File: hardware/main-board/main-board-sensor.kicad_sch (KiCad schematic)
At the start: 16 parts, among them J4 Conn_01x04, U1 TSL2585, U3 MIC4812, U7 MCP9808

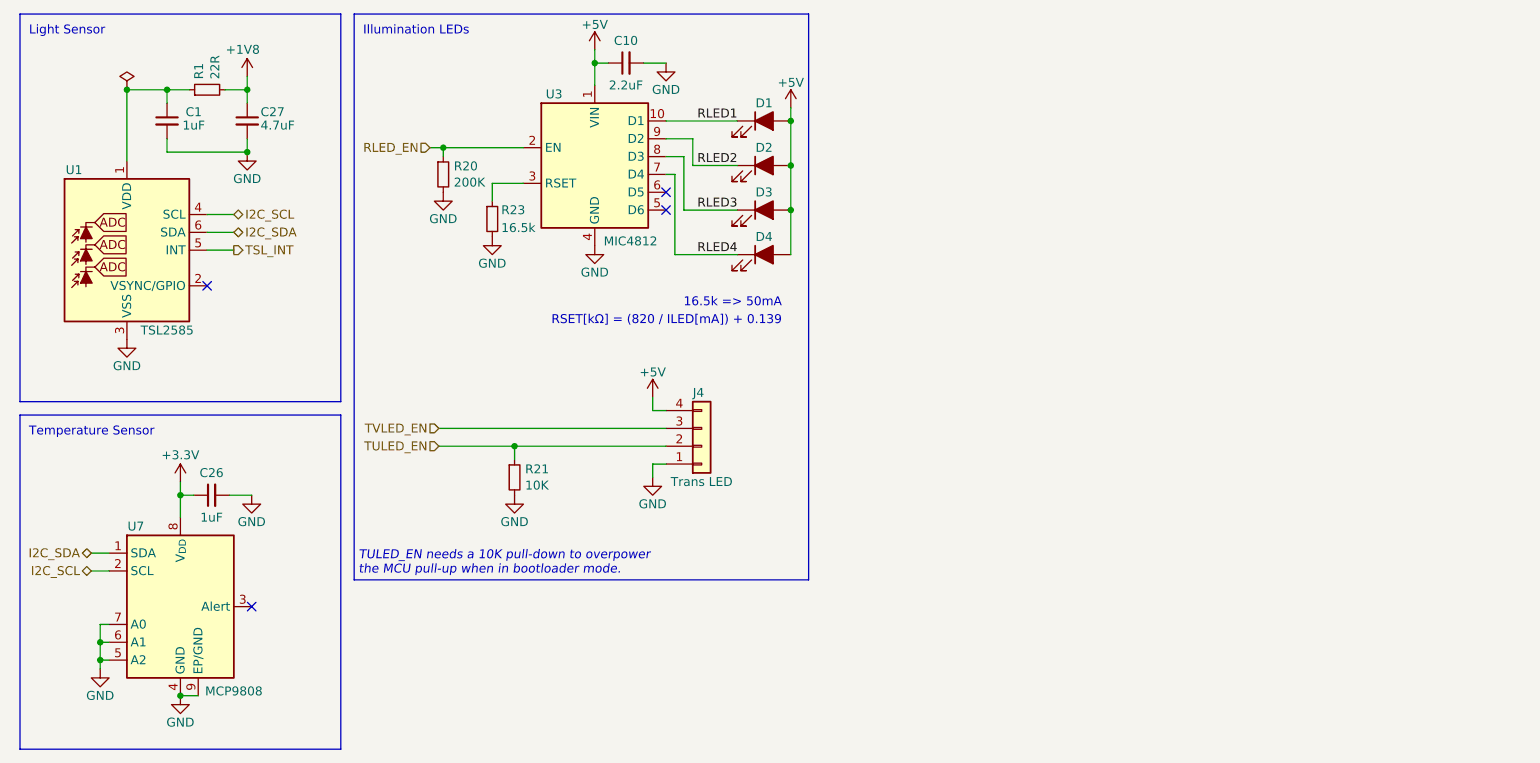
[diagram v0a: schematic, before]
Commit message: Implement VSYNC reference signal
Adds a 32.768kHz oscillator and a binary counter to divide it, providing
a stable 128Hz signal routed to the sensor's VSYNC pin.
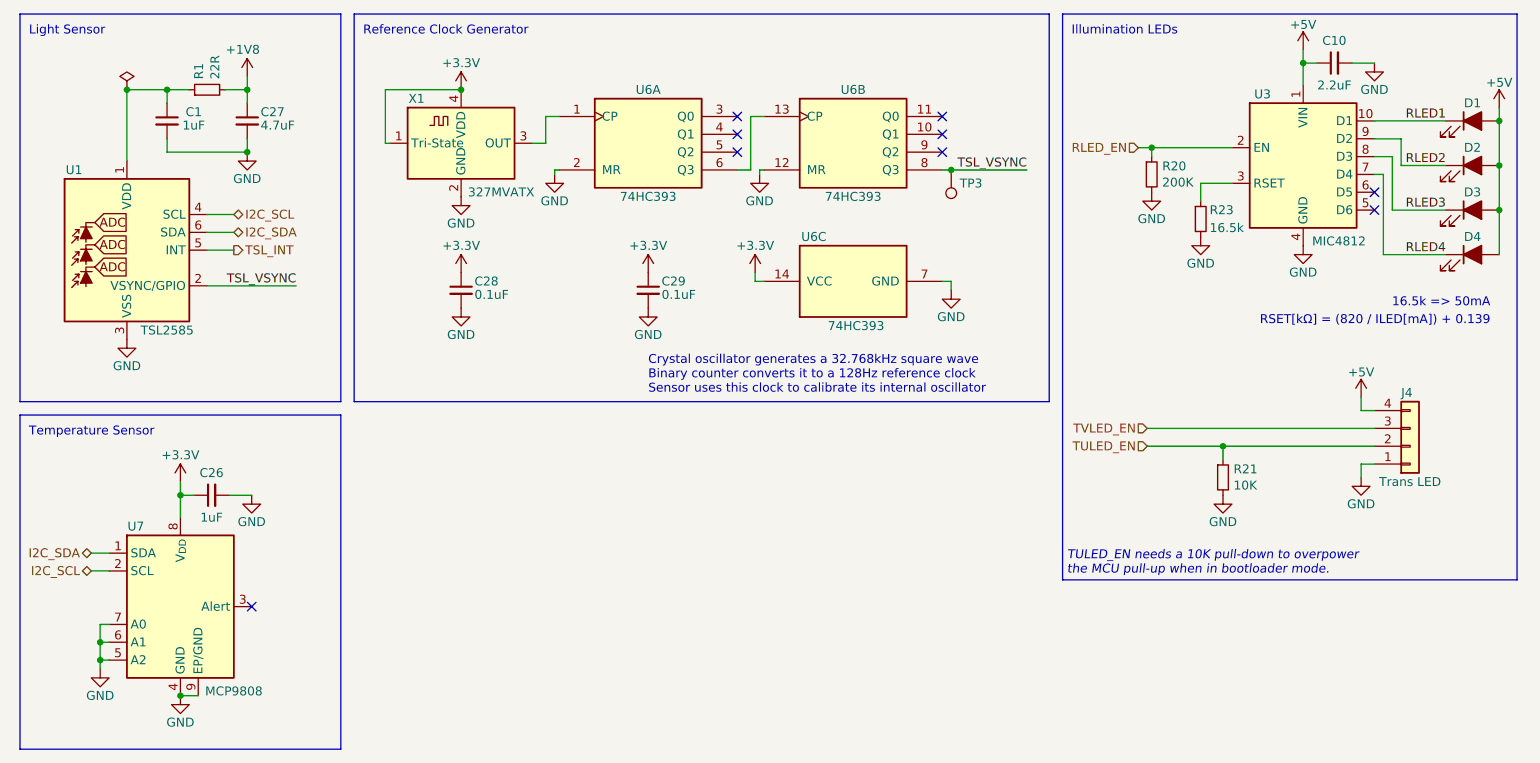
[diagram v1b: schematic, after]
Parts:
- added C28, C29: 0.1uF, Capacitor_SMD:C_0603_1608Metric, symbol Device:C_Small
- added TP3: 1.8V, TestPoint:TestPoint_Pad_D1.0mm, symbol Connector:TestPoint
- added U6: 74HC393, lib_fp:DHVQFN-14-1EP_2.5x3mm_P0.5mm_EP1x1.5mm, symbol 74xx:74LS393
- added X1: 327MVATX, lib_fp:Oscillator_SMD_ECS_327MVATX-2-4Pin_2.5x2.0mm, symbol Oscillator:ECS-2520MV-xxx-xx
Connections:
- net +3.3V: now also C28.1, C29.1, U6.14 (VCC), X1.1 (Tri-State), X1.4 (VDD)
- net GND: now also C28.2, C29.2, U6.12 (MR), U6.2 (MR), U6.7 (GND), X1.2 (GND)
- net TSL_VSYNC: now reaches U1.2 (VSYNC/GPIO)
- net TSL_VSYNC: now also TP3.1, U6.8 (Q3)
- new net: U6.13 (CP), U6.6 (Q3)
- new net: U6.1 (CP), X1.3 (OUT)
- no-connect marks 4 -> 9
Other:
- note added: "Crystal oscillator generates a 32.768kHz square wave Binary counter converts it to a 128Hz reference clock Sensor uses this clock to calibrate its internal oscillator"
- note added: "Reference Clock Generator"
- moved on the sheet: C10, D1, D2, D3, D4, J4, R20, R21, R23, U3

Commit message: Final tweaks for Rev C manufacture
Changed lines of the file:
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@@
 	(title_block
 		(title "Printalyzer UV/VIS Densitometer - Main Board")
-		(date "2024-09-04")
+		(date "2024-09-24")
 		(rev "C")
 		(company "Dektronics, Inc.")
@@
 	(rectangle
 		(start 163.195 14.605)
-		(end 227.965 95.25)
-		(stroke
-			(width 0)
+		(end 229.235 95.25)
+		(stroke
+			(width 0)

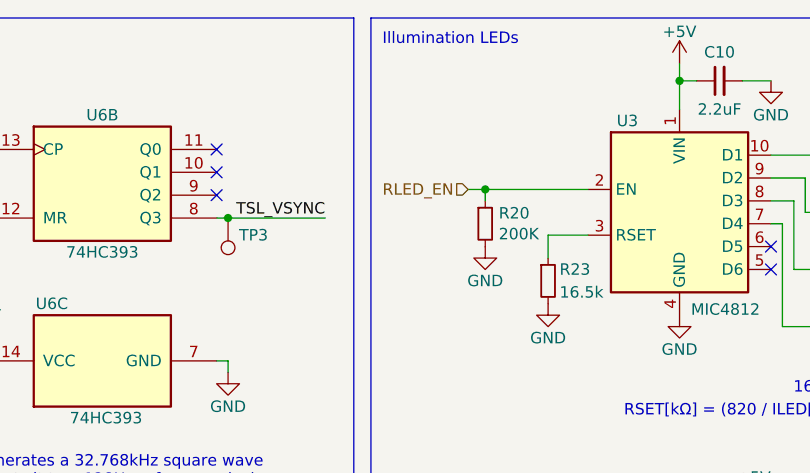
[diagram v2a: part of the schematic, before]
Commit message: Fix net name for reflection LEDs
This should match the identifer used in the firmware, for consistency
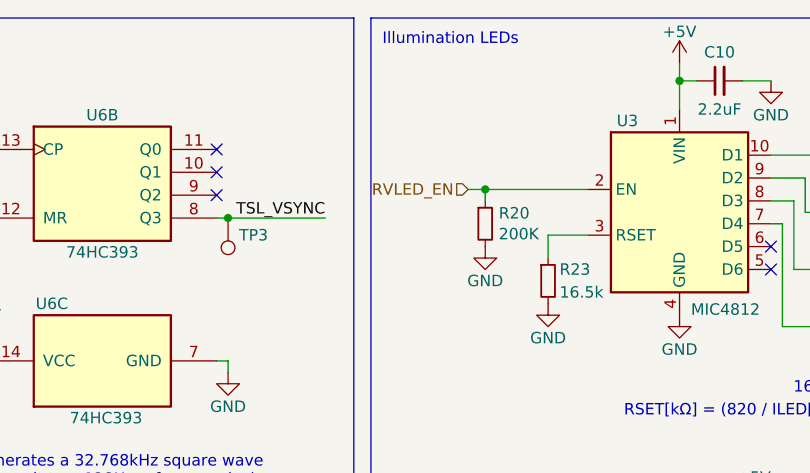
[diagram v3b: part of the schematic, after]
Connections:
- net RLED_EN renamed RVLED_EN
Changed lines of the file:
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@@
 		)
 	)
-	(hierarchical_label "RLED_EN"
+	(hierarchical_label "RVLED_EN"
 		(shape input)
 		(at 173.99 33.655 180)

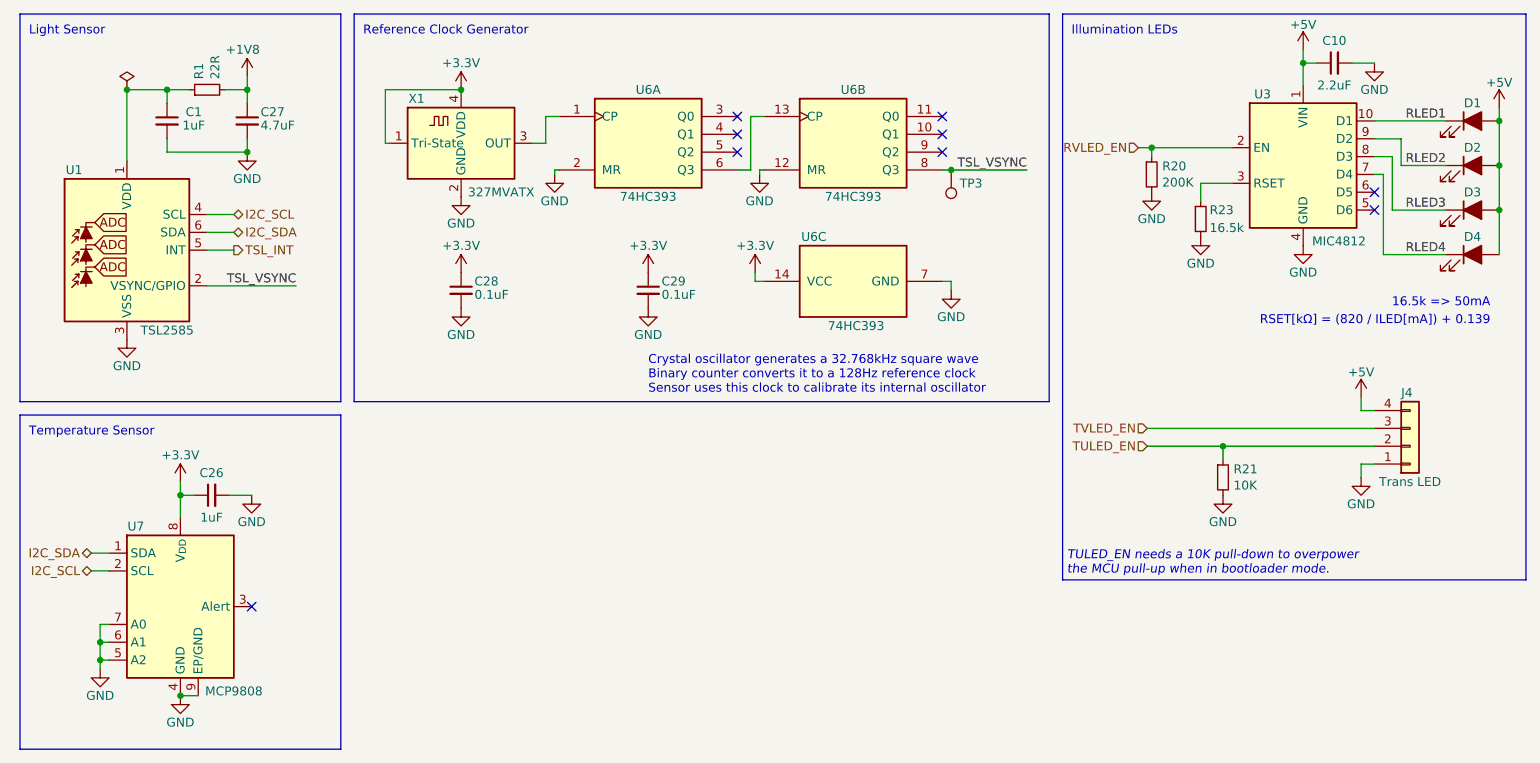
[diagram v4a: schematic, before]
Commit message: Remove crystal reference and reroute VSYNC pin
In testing with Rev C hardware, it was determined that using the VSYNC
pin to calibrate the TSL2585's internal oscillator can actually
introduce more instability in sensor timing than would otherwise exist.
Furthermore, the most likely factor affecting oscillator stability is
temperature, which we're already planning to correct for.

Thus these extra components should be removed from the design.

For the sake of future-proofing, the VSYNC pin is now rounded directly
to the MCU (though a pull-up resistor), in case someday it is decided to
use this as a measurement trigger. It is also likely this pin will never
be used, but it doesn't really hurt to do this.

Fix #2
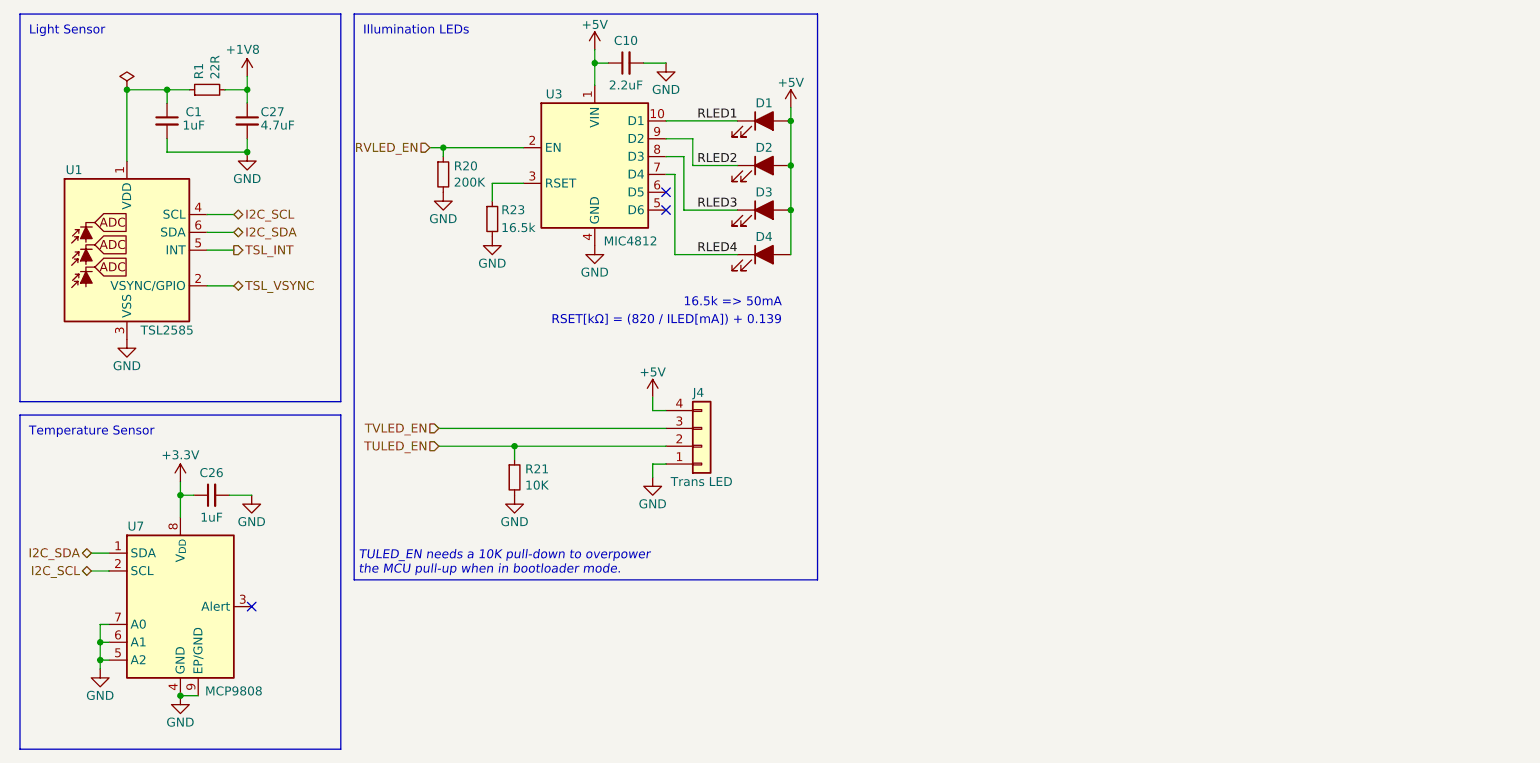
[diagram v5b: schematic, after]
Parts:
- removed C28, C29: 0.1uF, Capacitor_SMD:C_0603_1608Metric, symbol Device:C_Small
- removed TP3: 1.8V, TestPoint:TestPoint_Pad_D1.0mm, symbol Connector:TestPoint
- removed U6: 74HC393, lib_fp:DHVQFN-14-1EP_2.5x3mm_P0.5mm_EP1x1.5mm, symbol 74xx:74LS393
- removed X1: 327MVATX, lib_fp:Oscillator_SMD_ECS_327MVATX-2-4Pin_2.5x2.0mm, symbol Oscillator:ECS-2520MV-xxx-xx
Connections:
- no-connect marks 9 -> 3
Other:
- note removed: "Crystal oscillator generates a 32.768kHz square wave Binary counter converts it to a 128Hz reference clock Sensor uses this clock to calibrate its internal oscillator"
- note removed: "Reference Clock Generator"
- moved on the sheet: C10, D1, D2, D3, D4, J4, R20, R21, R23, U3
